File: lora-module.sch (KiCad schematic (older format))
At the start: 36 parts, among them J1 RF_Shield_One_Piece, P1 CONN_01X07, P2 CONN_01X07, Q1 32MHz, U2 SX1276, U5 PE4259

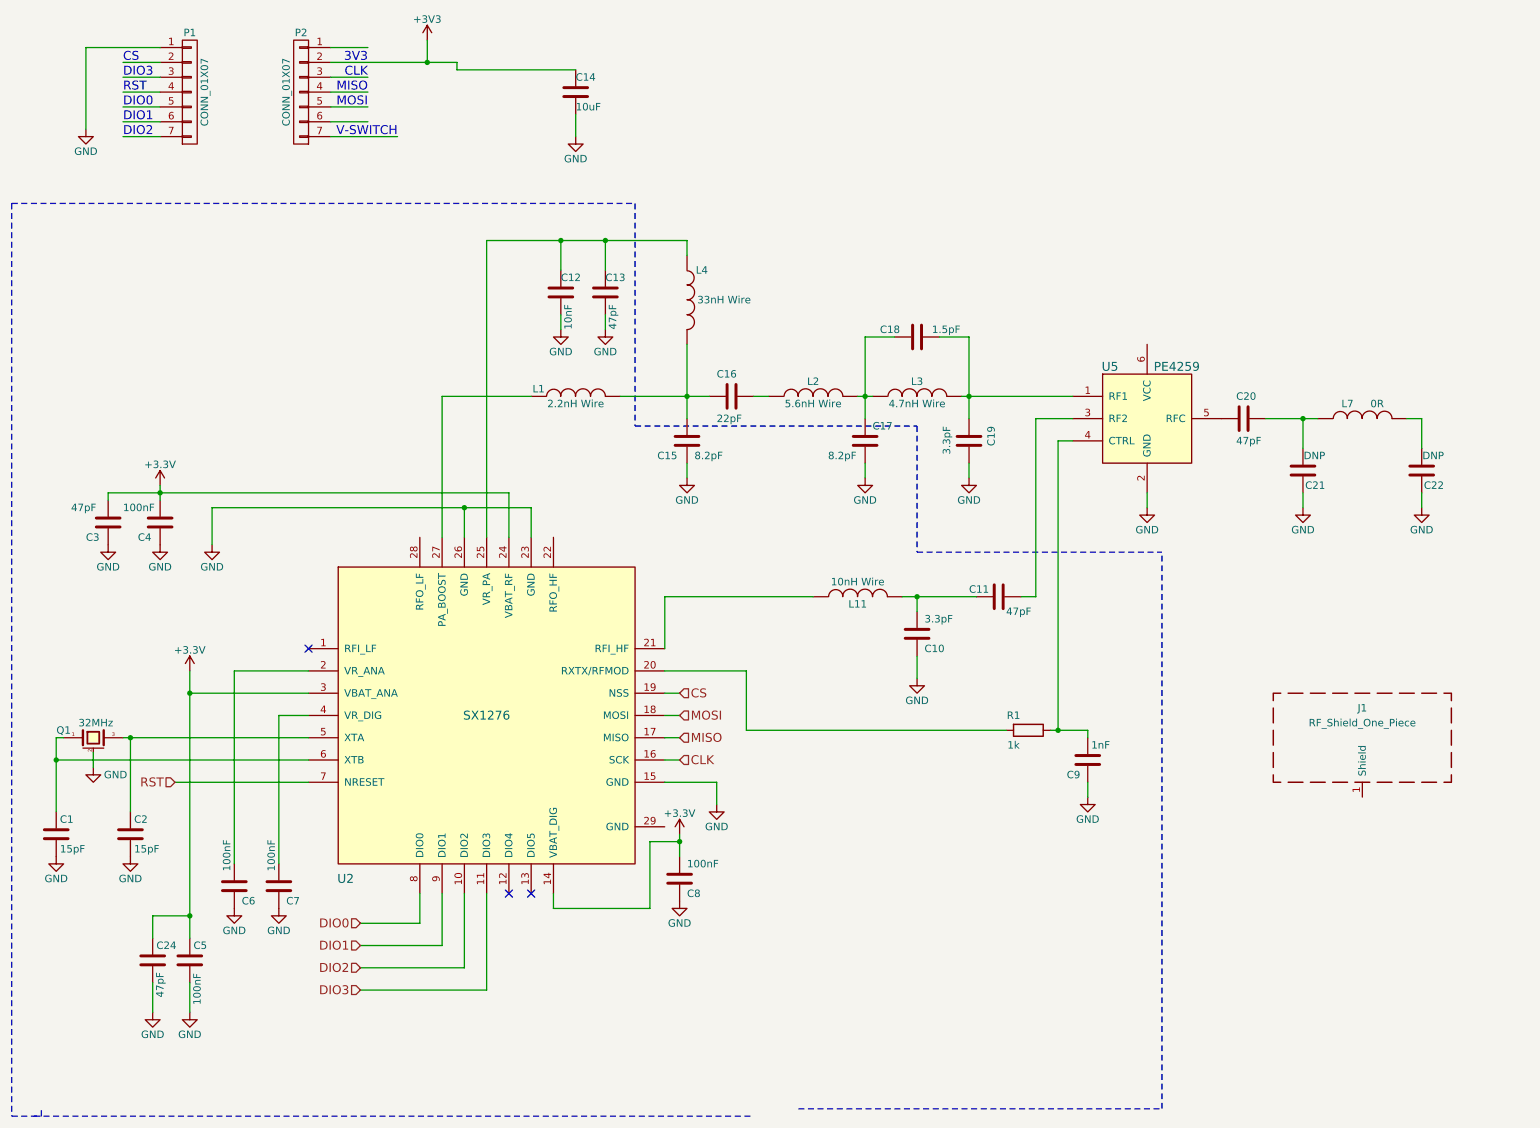
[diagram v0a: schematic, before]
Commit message: added most of components to PCB
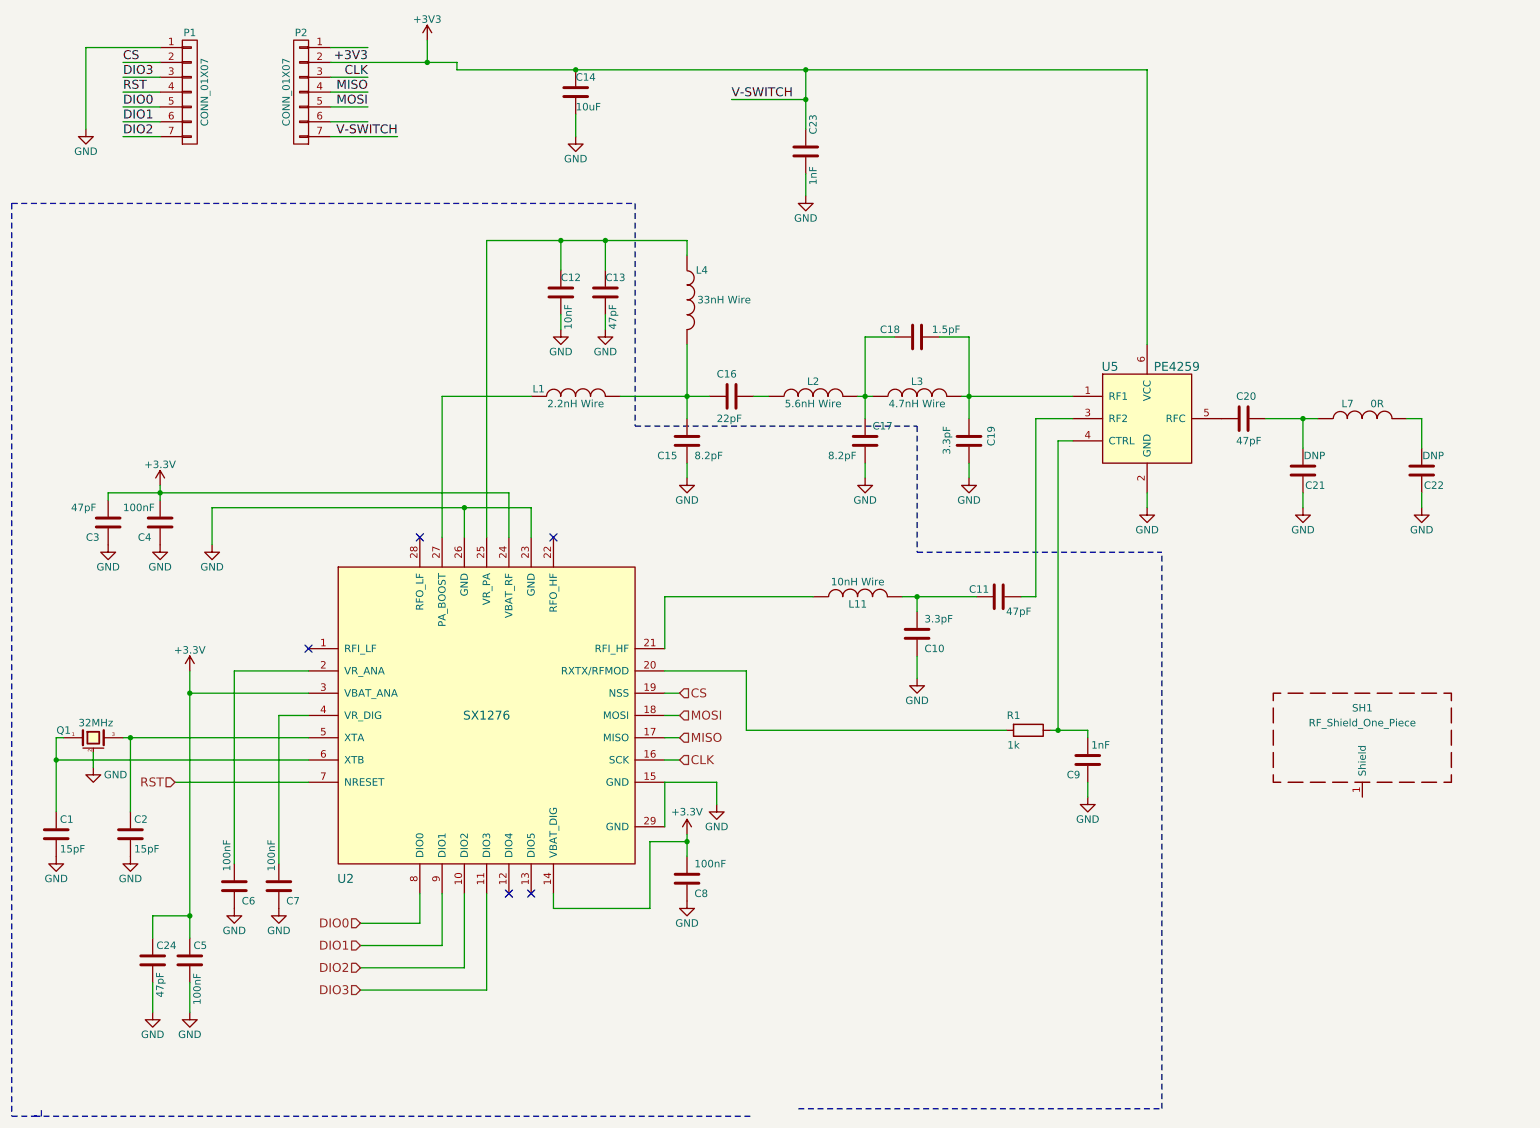
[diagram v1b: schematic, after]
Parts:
- added C23: 1nF, Capacitors_SMD:C_0402, symbol C
- C10, C11, C12, C13, C15, C16, C17, C18, C19, C20, C21, C22, C24, C3, C4, C5, C6, C7, C8, C9: footprint (none) -> Capacitors_SMD:C_0402
- L1, L11, L2, L3, L4, L7: footprint (none) -> Inductors_SMD:L_0402
- R1: footprint (none) -> Resistors_SMD:R_0402
- SH1: renamed from J1; footprint (none) -> balcerzak-pcb:inAIR9B_shield
- U2: footprint (none) -> Housings_DFN_QFN:QFN-28-1EP_6x6mm_Pitch0.65mm
- U5: footprint (none) -> TO_SOT_Packages_SMD:SOT-363_SC-70-6
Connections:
- net labels added: V-SWITCH
- wire segments 107 -> 112
- no-connect marks 3 -> 5
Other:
- note removed: "3V3"
- note removed: "CLK"
- note removed: "CS"
- note removed: "DIO0"
- note removed: "DIO1"
- note removed: "DIO2"
- note removed: "DIO3"
- note removed: "MISO"
- note removed: "MOSI"
- note removed: "RST"
- note removed: "V-SWITCH"
- moved on the sheet: C8

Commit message: added all components description
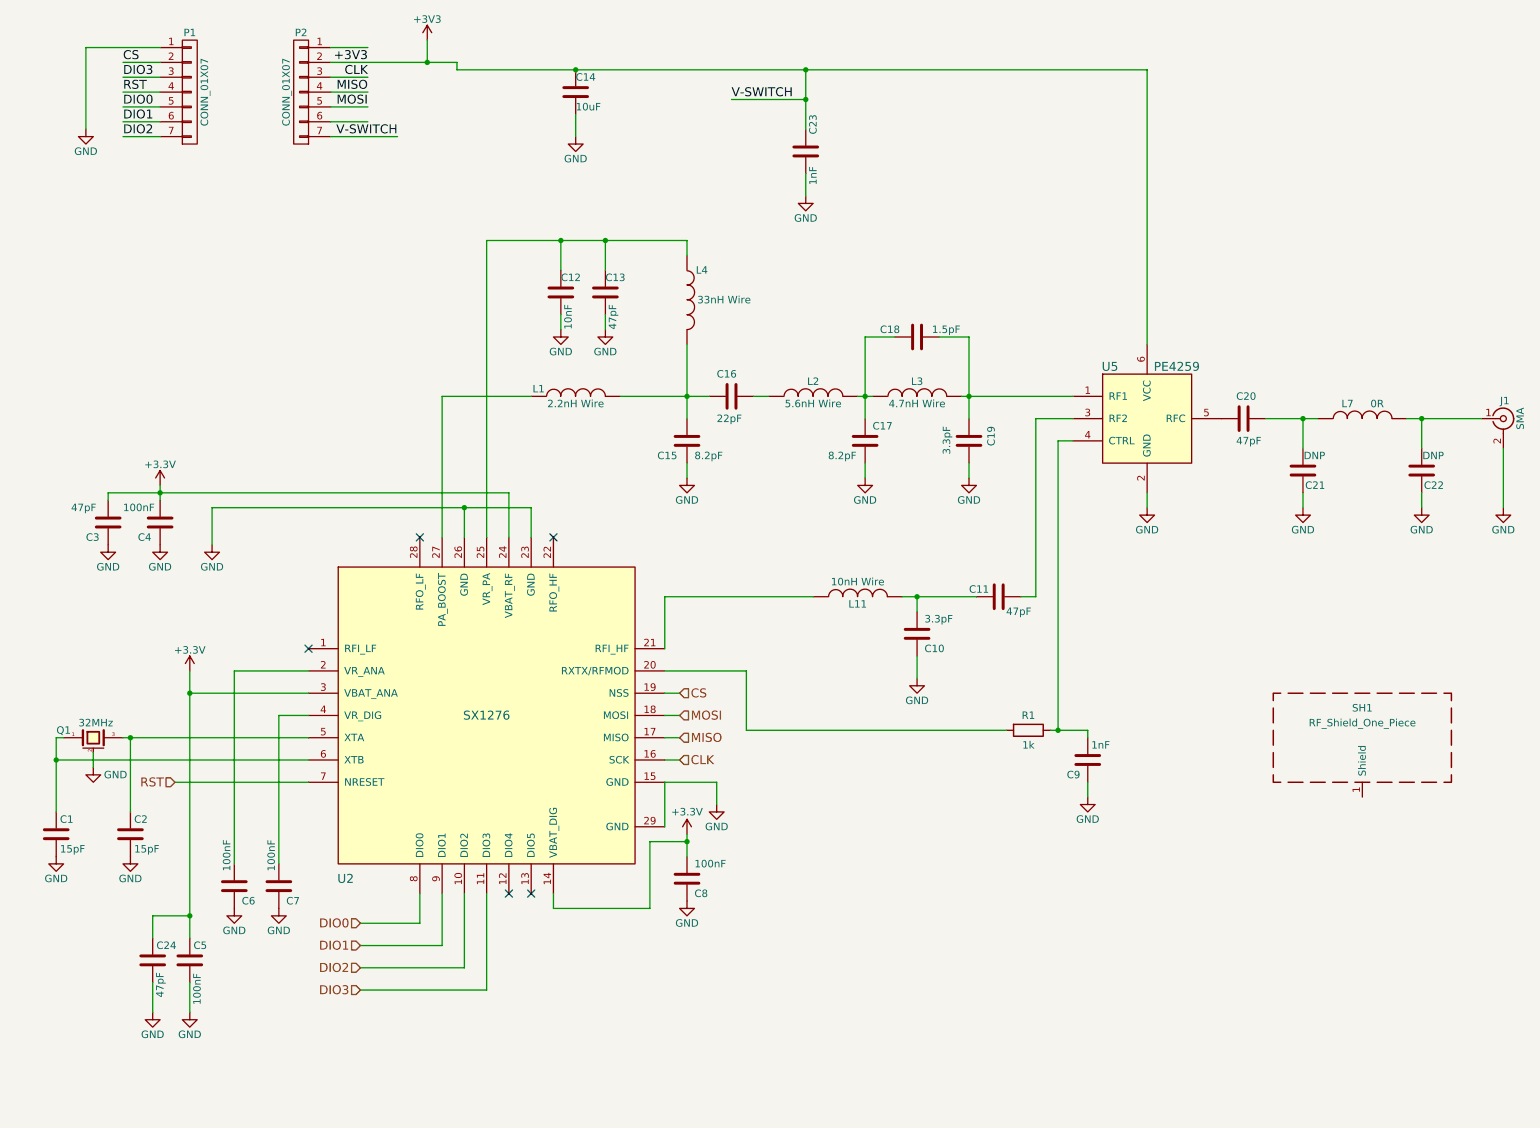
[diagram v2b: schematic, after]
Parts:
- added J1: SMA, symbol CONN_COAXIAL
- C16: Link (none) -> https://www.tme.eu/pl/details/grm1555c1h220ja01d/kondensato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; Manufacturer (none) -> MURATA; Name (none) -> GRM1555C1H220JA01D
- C18: Link (none) -> https://www.tme.eu/pl/details/cc0402crnpo91r5/kondensatory-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; Manufacturer (none) -> YAGEO; Name (none) -> CC0402CRNPO9BN1R5
- C19: Link (none) -> https://www.tme.eu/pl/details/cl05c3r3cb5nnnc/kondensatory-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; Manufacturer (none) -> SAMSUNG; Name (none) -> CL05C3R3CB5NNNC
- C20: Link (none) -> https://www.tme.eu/pl/details/grm1555c1h470ja01d/kondensato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; Manufacturer (none) -> MURATA; Name (none) -> GRM1555C1H470JA01D
- C23: Link (none) -> https://www.tme.eu/pl/details/vj0402y102kxacw2bc/kondensato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; Manufacturer (none) -> VISHAY; Name (none) -> VJ0402Y102KXACW2BC
- L2: Link (none) -> https://www.tme.eu/pl/details/lqw15an5n6c10d/dlawiki-smd-04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; Manufacturer (none) -> MURATA; Name (none) -> LQW15AN5N6C10D
- L3: Link (none) -> https://www.tme.eu/pl/details/cw0402-4.7/cewki-smd/ferrocor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; Manufacturer (none) -> FERROCORE; Name (none) -> CW0402-4.7
- L4: Link (none) -> http://pl.farnell.com/te-connectivity/3-2176086-7/inductor-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; Manufacturer (none) -> TE CONNECTIVITY; Name (none) -> 3-2176086-7
- P1, P2: Link (none) -> https://www.tme.eu/pl/details/mx-90120-0767/listwy-i-gniazd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; Manufacturer (none) -> MOLEX; Name (none) -> 901200767
- U2: Link (none) -> http://pl.mouser.com/ProductDetail/Semtech/SX1276IMLTRT/?qs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; Manufacturer (none) -> SEMTECH; Name (none) -> SX1276
- U5: Link (none) -> https://www.digikey.com/products/en/rf-if-and-rfid/rf-switc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; Manufacturer (none) -> Peregrine Semiconductor; Name (none) -> PE4259
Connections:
- net GND: now also J1.2 (Ext)
- net at C22.2, L7.2: now also J1.1 (In)
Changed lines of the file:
@@
 encoding utf-8
 Sheet 1 1
-Title ""
-Date ""
-Rev ""
+Title "LoRA module"
+Date "2017-09-30"
+Rev "1.0"
 Comp ""
 Comment1 ""
@@
 F 2 "Inductors_SMD:L_0402" H 4850 2500 50  0001 C CNN
 F 3 "" H 4850 2500 50  0000 C CNN
+F 4 "http://pl.farnell.com/te-connectivity/3-2176086-7/inductor-0402-33nh-5/dp/2116085" H 4850 2500 60  0001 C CNN "Link"
+F 5 "3-2176086-7" H 4850 2500 60  0001 C CNN "Name"
+F 6 "TE CONNECTIVITY" H 4850 2500 60  0001 C CNN "Manufacturer"
 	1    4850 2500
 	1    0    0    -1
@@
 F 2 "Capacitors_SMD:C_0402" H 5188 3000 50  0001 C CNN
 F 3 "" H 5150 3150 50  0000 C CNN
+F 4 "MURATA" V 5150 3150 60  0001 C CNN "Manufacturer"
+F 5 "GRM1555C1H220JA01D" V 5150 3150 60  0001 C CNN "Name"
+F 6 "https://www.tme.eu/pl/details/grm1555c1h220ja01d/kondensatory-mlcc-smd-0402/murata/" V 5150 3150 60  0001 C CNN "Link"
 	1    5150 3150
 	0    1    1    0
@@
 F 2 "Inductors_SMD:L_0402" H 5700 3150 50  0001 C CNN
 F 3 "" H 5700 3150 50  0000 C CNN
+F 4 "https://www.tme.eu/pl/details/lqw15an5n6c10d/dlawiki-smd-0402/murata/" V 5700 3150 60  0001 C CNN "Link"
+F 5 "MURATA" V 5700 3150 60  0001 C CNN "Manufacturer"
+F 6 "LQW15AN5N6C10D" V 5700 3150 60  0001 C CNN "Name"
 	1    5700 3150
 	0    -1   -1   0
@@
 F 2 "Inductors_SMD:L_0402" H 6400 3150 50  0001 C CNN
 F 3 "" H 6400 3150 50  0000 C CNN
+F 4 "FERROCORE" V 6400 3150 60  0001 C CNN "Manufacturer"
+F 5 "CW0402-4.7" V 6400 3150 60  0001 C CNN "Name"
+F 6 "https://www.tme.eu/pl/details/cw0402-4.7/cewki-smd/ferrocore/" V 6400 3150 60  0001 C CNN "Link"
 	1    6400 3150
 	0    -1   -1   0
@@
 F 2 "Capacitors_SMD:C_0402" H 6438 2600 50  0001 C CNN
 F 3 "" H 6400 2750 50  0000 C CNN
+F 4 "https://www.tme.eu/pl/details/cc0402crnpo91r5/kondensatory-mlcc-smd-0402/yageo/cc0402crnpo9bn1r5/" V 6400 2750 60  0001 C CNN "Link"
+F 5 "YAGEO" V 6400 2750 60  0001 C CNN "Manufacturer"
+F 6 "CC0402CRNPO9BN1R5" V 6400 2750 60  0001 C CNN "Name"
 	1    6400 2750
 	0    1    1    0
@@
 F 2 "Capacitors_SMD:C_0402" H 6788 3300 50  0001 C CNN
 F 3 "" H 6750 3450 50  0000 C CNN
+F 4 "https://www.tme.eu/pl/details/cl05c3r3cb5nnnc/kondensatory-mlcc-smd-0402/samsung/" V 6750 3450 60  0001 C CNN "Link"
+F 5 "CL05C3R3CB5NNNC" V 6750 3450 60  0001 C CNN "Name"
+F 6 "SAMSUNG" V 6750 3450 60  0001 C CNN "Manufacturer"
 	1    6750 3450
 	-1   0    0    1
@@
 U 1 1 58FFF26B
 P 7150 5400
-F 0 "R1" V 7050 5300 50  0000 C CNN
-F 1 "1k" V 7250 5300 50  0000 C CNN
+F 0 "R1" V 7050 5400 50  0000 C CNN
+F 1 "1k" V 7250 5400 50  0000 C CNN
 F 2 "Resistors_SMD:R_0402" V 7080 5400 50  0001 C CNN
 F 3 "" H 7150 5400 50  0000 C CNN
@@
 F 2 "Pin_Headers:Pin_Header_Straight_1x07_Pitch2.54mm" H 1500 1100 50  0001 C CNN
 F 3 "" H 1500 1100 50  0000 C CNN
+F 4 "https://www.tme.eu/pl/details/mx-90120-0767/listwy-i-gniazda-kolkowe/molex/901200767/" H 1500 1100 60  0001 C CNN "Link"
+F 5 "MOLEX" H 1500 1100 60  0001 C CNN "Manufacturer"
+F 6 "901200767" H 1500 1100 60  0001 C CNN "Name"
 	1    1500 1100
 	1    0    0    -1
@@
 F 2 "Pin_Headers:Pin_Header_Straight_1x07_Pitch2.54mm" H 2250 1100 50  0001 C CNN
 F 3 "" H 2250 1100 50  0000 C CNN
+F 4 "901200767" H 2250 1100 60  0001 C CNN "Name"
+F 5 "MOLEX" H 2250 1100 60  0001 C CNN "Manufacturer"
+F 6 "https://www.tme.eu/pl/details/mx-90120-0767/listwy-i-gniazda-kolkowe/molex/901200767/" H 2250 1100 60  0001 C CNN "Link"
 	1    2250 1100
 	-1   0    0    -1
@@
 F 2 "Capacitors_SMD:C_0402" H 8638 3150 50  0001 C CNN
 F 3 "" H 8600 3300 50  0000 C CNN
+F 4 "GRM1555C1H470JA01D" V 8600 3300 60  0001 C CNN "Name"
+F 5 "MURATA" V 8600 3300 60  0001 C CNN "Manufacturer"
+F 6 "https://www.tme.eu/pl/details/grm1555c1h470ja01d/kondensatory-mlcc-smd-0402/murata/" V 8600 3300 60  0001 C CNN "Link"
 	1    8600 3300
 	0    1    1    0
@@
 	9800 3500 9800 3300
 Wire Wire Line
-	9800 3300 9700 3300
+	9700 3300 10200 3300
 Connection ~ 6400 4500
 Wire Wire Line
@@
 	1    0    0    -1
 $EndComp
-Wire Notes Line
-	450  8000 5300 8000
-Wire Notes Line
-	300  1850 300  8000
-Wire Notes Line
-	300  8000 500  8000
-Wire Notes Line
-	500  8000 500  7950
 $Comp
 L C C13
@@
 $EndComp
 Connection ~ 7350 5400
-Wire Notes Line
-	5600 7950 8050 7950
-Wire Notes Line
-	8050 7950 8050 4200
 $Comp
 L INDUCTOR L1
@@
 	0    -1   -1   0
 $EndComp
-Wire Notes Line
-	300  1850 4500 1850
-Wire Notes Line
-	4500 1850 4500 3350
 $Comp
 L C C17
@@
 	1    0    0    -1
 $EndComp
-Wire Notes Line
-	4500 3350 6400 3350
-Wire Notes Line
-	6400 3350 6400 4200
-Wire Notes Line
-	6400 4200 8050 4200
 Wire Wire Line
 	800  800  1300 800
@@
 F 2 "Housings_DFN_QFN:QFN-28-1EP_6x6mm_Pitch0.65mm" H 3200 5300 60  0001 C CNN
 F 3 "" H 3200 5300 60  0001 C CNN
+F 4 "SEMTECH" H 3500 5300 60  0001 C CNN "Manufacturer"
+F 5 "http://pl.mouser.com/ProductDetail/Semtech/SX1276IMLTRT/?qs=sGAEpiMZZMtzPgOfznR9QX5rqU4bc2QM6PQA53z5lyI%3d" H 3500 5300 60  0001 C CNN "Link"
+F 6 "SX1276" H 3500 5300 60  0001 C CNN "Name"
 	1    3500 5300
 	1    0    0    -1
@@
 F 2 "TO_SOT_Packages_SMD:SOT-363_SC-70-6" H 8350 3000 60  0001 C CNN
 F 3 "" H 8350 3000 60  0001 C CNN
+F 4 "https://www.digikey.com/products/en/rf-if-and-rfid/rf-switches/865?k=PE4259" H 7950 3300 60  0001 C CNN "Link"
+F 5 "Peregrine Semiconductor" H 7950 3300 60  0001 C CNN "Manufacturer"
+F 6 "PE4259" H 7950 3300 60  0001 C CNN "Name"
 	1    7950 3300
 	1    0    0    -1
@@
 F 2 "Capacitors_SMD:C_0402" H 5688 1350 50  0001 C CNN
 F 3 "" H 5650 1500 50  0000 C CNN
+F 4 "VISHAY" V 5650 1500 60  0001 C CNN "Manufacturer"
+F 5 "https://www.tme.eu/pl/details/vj0402y102kxacw2bc/kondensatory-mlcc-smd-0402/vishay/" V 5650 1500 60  0001 C CNN "Link"
+F 6 "VJ0402Y102KXACW2BC" V 5650 1500 60  0001 C CNN "Name"
 	1    5650 1500
 	-1   0    0    1
@@
 Connection ~ 4100 950
 $Comp
-L GND #PWR?
+L GND #PWR029
 U 1 1 59935F61
 P 5650 1800
-F 0 "#PWR?" H 5650 1550 50  0001 C CNN
+F 0 "#PWR029" H 5650 1550 50  0001 C CNN
 F 1 "GND" H 5650 1650 50  0000 C CNN
 F 2 "" H 5650 1800 50  0001 C CNN
@@
 Text Label 5150 1150 0    60   ~ 0
 V-SWITCH
+$Comp
+L CONN_COAXIAL J1
+U 1 1 59CF40CD
+P 10350 3300
+F 0 "J1" H 10360 3420 50  0000 C CNN
+F 1 "SMA" V 10465 3300 50  0000 C CNN
+F 2 "" H 10350 3300 50  0001 C CNN
+F 3 "" H 10350 3300 50  0001 C CNN
+	1    10350 3300
+	1    0    0    -1
+$EndComp
+Connection ~ 9800 3300
+$Comp
+L GND #PWR030
+U 1 1 59CF457A
+P 10350 3900
+F 0 "#PWR030" H 10350 3650 50  0001 C CNN
+F 1 "GND" H 10350 3750 50  0000 C CNN
+F 2 "" H 10350 3900 50  0000 C CNN
+F 3 "" H 10350 3900 50  0000 C CNN
+	1    10350 3900
+	1    0    0    -1
+$EndComp
+Wire Wire Line
+	10350 3500 10350 3900
 $EndSCHEMATC
